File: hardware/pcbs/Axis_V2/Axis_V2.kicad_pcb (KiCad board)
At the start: 2 copper layers, 86.4 x 66 mm, 28 parts, among them J1 SWD, J2 UART, J3 Conn_01x02, J4 Conn_01x02, J5 Conn_01x04, J6 Conn_01x10, J7 Conn_01x08, SW1 RES, U1 Pico, U2 MAX31855EASA, U3 MAX31855EASA, U4 MAX6107, U5 FM24CL16B, U6 ADS1119IPWR, U7 TCA9534

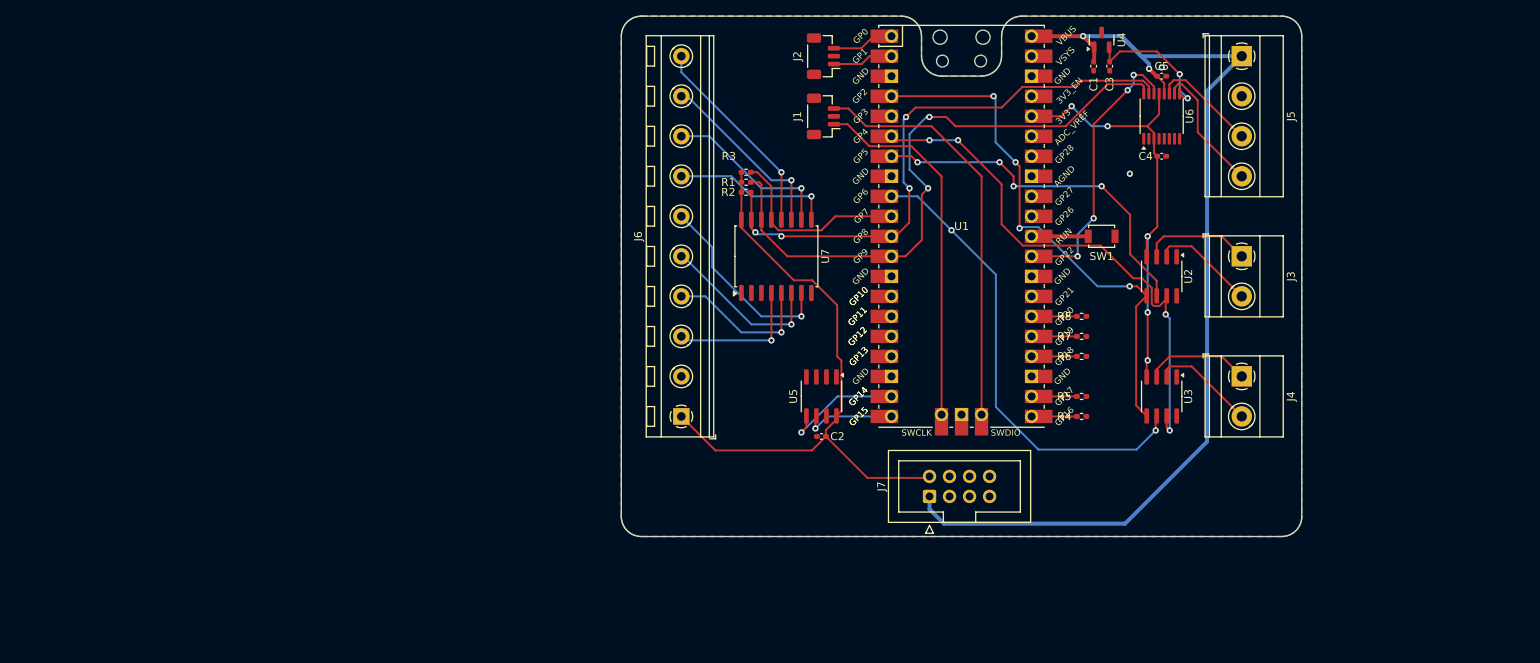
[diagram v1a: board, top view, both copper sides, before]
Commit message: Added a I2C expander for non-essential peripherals, etc.
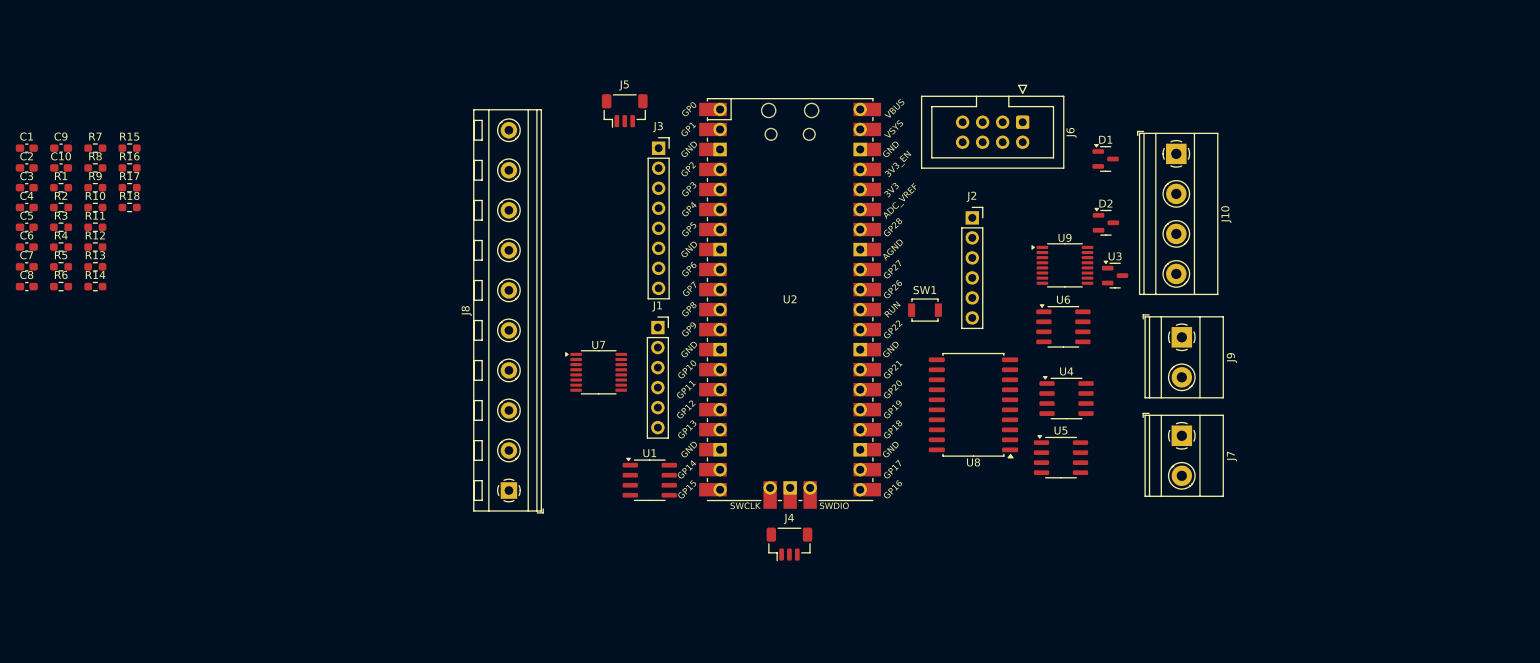
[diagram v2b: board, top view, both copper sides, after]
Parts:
- added C10: 0.1u, Capacitor_SMD:C_0603_1608Metric_Pad1.08x0.95mm_HandSolder, F.Cu at (-13.6, 39.3)
- added C6: 0.1u, Capacitor_SMD:C_0603_1608Metric_Pad1.08x0.95mm_HandSolder, F.Cu at (-18.0, 49.3)
- added C7: 0.1u, Capacitor_SMD:C_0603_1608Metric_Pad1.08x0.95mm_HandSolder, F.Cu at (-18.0, 51.8)
- added C8: 0.1u, Capacitor_SMD:C_0603_1608Metric_Pad1.08x0.95mm_HandSolder, F.Cu at (-18.0, 54.3)
- added C9: 0.1u, Capacitor_SMD:C_0603_1608Metric_Pad1.08x0.95mm_HandSolder, F.Cu at (-13.6, 36.8)
- added D1: 4.7v, Package_TO_SOT_SMD:SOT-23, F.Cu at (118.9, 38.1)
- added D2: 4.7v, Package_TO_SOT_SMD:SOT-23, F.Cu at (119.0, 46.2)
- added J10: Conn_01x04, TerminalBlock_Phoenix:TerminalBlock_Phoenix_MKDS-1,5-4-5.08_1x04_P5.08mm_Horizontal, F.Cu at (127.9, 37.5)
- added J8: Conn_01x10, TerminalBlock_RND:TerminalBlock_RND_205-00240_1x10_P5.08mm_Horizontal, F.Cu at (43.2, 80.2)
- added J9: Conn_01x02, TerminalBlock_Phoenix:TerminalBlock_Phoenix_MKDS-1,5-2-5.08_1x02_P5.08mm_Horizontal, F.Cu at (128.6, 60.8)
- added R10: 1k, Resistor_SMD:R_0603_1608Metric_Pad0.98x0.95mm_HandSolder, F.Cu at (-9.29, 44.3)
- added R11: 1k, Resistor_SMD:R_0603_1608Metric_Pad0.98x0.95mm_HandSolder, F.Cu at (-9.29, 46.8)
- added R12: 1k, Resistor_SMD:R_0603_1608Metric_Pad0.98x0.95mm_HandSolder, F.Cu at (-9.29, 49.3)
- added R13: 1k, Resistor_SMD:R_0603_1608Metric_Pad0.98x0.95mm_HandSolder, F.Cu at (-9.29, 51.8)
- added R14: 1k, Resistor_SMD:R_0603_1608Metric_Pad0.98x0.95mm_HandSolder, F.Cu at (-9.29, 54.3)
- added R15: 1k, Resistor_SMD:R_0603_1608Metric_Pad0.98x0.95mm_HandSolder, F.Cu at (-4.94, 36.8)
- added R16: 1k, Resistor_SMD:R_0603_1608Metric_Pad0.98x0.95mm_HandSolder, F.Cu at (-4.94, 39.3)
- added R17: 1k, Resistor_SMD:R_0603_1608Metric_Pad0.98x0.95mm_HandSolder, F.Cu at (-4.94, 41.8)
- added R18: 1k, Resistor_SMD:R_0603_1608Metric_Pad0.98x0.95mm_HandSolder, F.Cu at (-4.94, 44.3)
- added R9: 1k, Resistor_SMD:R_0603_1608Metric_Pad0.98x0.95mm_HandSolder, F.Cu at (-9.29, 41.8)
- added U8: PCA9544AD, Package_SO:SOIC-20W_7.5x12.8mm_P1.27mm, F.Cu at (102.2, 69.3)
- added U9: ADS1119IPWR, Package_SO:TSSOP-16_4.4x5mm_P0.65mm, F.Cu at (113.8, 51.6)
- C1, C2, C3, C4, C5: footprint Capacitor_SMD:C_0402_1005Metric_Pad0.74x0.62mm_HandSolder -> Capacitor_SMD:C_0603_1608Metric_Pad1.08x0.95mm_HandSolder
- J1: value SWD -> EXT_SPI; footprint Connector_JST:JST_SH_BM03B-SRSS-TB_1x03-1MP_P1.00mm_Vertical -> Connector_PinSocket_2.54mm:PinSocket_1x06_P2.54mm_Vertical
- J2: value UART -> EXT_I2C; footprint Connector_JST:JST_SH_BM03B-SRSS-TB_1x03-1MP_P1.00mm_Vertical -> Connector_PinSocket_2.54mm:PinSocket_1x06_P2.54mm_Vertical
- J3: value Conn_01x02 -> GPIO; footprint TerminalBlock_Phoenix:TerminalBlock_Phoenix_MKDS-1,5-2-5.08_1x02_P5.08mm_Horizontal -> Connector_PinSocket_2.54mm:PinSocket_1x08_P2.54mm_Vertical
- J4: value Conn_01x02 -> SWD; footprint TerminalBlock_Phoenix:TerminalBlock_Phoenix_MKDS-1,5-2-5.08_1x02_P5.08mm_Horizontal -> Connector_JST:JST_SH_BM03B-SRSS-TB_1x03-1MP_P1.00mm_Vertical
- J5: value Conn_01x04 -> UART; footprint TerminalBlock_Phoenix:TerminalBlock_Phoenix_MKDS-1,5-4-5.08_1x04_P5.08mm_Horizontal -> Connector_JST:JST_SH_BM03B-SRSS-TB_1x03-1MP_P1.00mm_Vertical
- J6: value Conn_01x10 -> HV_IDC; footprint TerminalBlock_RND:TerminalBlock_RND_205-00240_1x10_P5.08mm_Horizontal -> Connector_IDC:IDC-Header_2x04_P2.54mm_Vertical
- J7: value Conn_01x08 -> Conn_01x02; footprint Connector_IDC:IDC-Header_2x04_P2.54mm_Vertical -> TerminalBlock_Phoenix:TerminalBlock_Phoenix_MKDS-1,5-2-5.08_1x02_P5.08mm_Horizontal
- R1, R2, R3, R4, R5, R6, R7, R8: footprint Resistor_SMD:R_0402_1005Metric_Pad0.72x0.64mm_HandSolder -> Resistor_SMD:R_0603_1608Metric_Pad0.98x0.95mm_HandSolder
- U1: value Pico -> FM24CL16B; footprint MCU_RaspberryPi_and_Boards:RPi_Pico_SMD_TH -> Package_SO:SOIC-8_3.9x4.9mm_P1.27mm
- U2: value MAX31855EASA -> Pico; footprint Package_SO:SOIC-8_3.9x4.9mm_P1.27mm -> MCU_RaspberryPi_and_Boards:RPi_Pico_SMD_TH
- U3: value MAX31855EASA -> MAX6107; footprint Package_SO:SOIC-8_3.9x4.9mm_P1.27mm -> Package_TO_SOT_SMD:SOT-23
- U4: value MAX6107 -> MAX31855EASA; footprint Package_TO_SOT_SMD:SOT-23 -> Package_SO:SOIC-8_3.9x4.9mm_P1.27mm
- U5: value FM24CL16B -> MAX31855EASA
- U6: value ADS1119IPWR -> DS3231MZ; footprint Package_SO:TSSOP-16_4.4x5mm_P0.65mm -> Package_SO:SOIC-8_3.9x4.9mm_P1.27mm
- U7: footprint Package_SO:SOIC-16W_7.5x10.3mm_P1.27mm -> Package_SO:TSSOP-16_4.4x5mm_P0.65mm
- moved C5 145.3 mm to (-18.0, 46.8)
- moved C4 144.2 mm to (-18.0, 44.3)
- moved C3 138.3 mm to (-18.0, 41.8), turned to 0 degrees
- moved C1 135.8 mm to (-18.0, 36.8), turned to 0 degrees
- moved R4 131.3 mm to (-13.6, 49.3), turned to 0 degrees
- moved R5 130.6 mm to (-13.6, 51.8), turned to 0 degrees
- moved R6 129.8 mm to (-13.6, 54.3), turned to 0 degrees
- moved R7 127.4 mm to (-9.29, 36.8), turned to 0 degrees
- moved R8 126.6 mm to (-9.29, 39.3), turned to 0 degrees
- moved C2 106.5 mm to (-18.0, 39.3), turned to 0 degrees
- moved R3 87.2 mm to (-13.6, 46.8)
- moved R2 87.0 mm to (-13.6, 44.3)
- moved R1 86.9 mm to (-13.6, 41.8)
- moved J5 78.6 mm to (57.9, 32.0), turned to 0 degrees
- moved J3 75.3 mm to (62.2, 36.8), turned to 0 degrees
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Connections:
- net /ADC_3 renamed +BATT
- C1 pad 1: +5V -> +3V3
- C2 pad 1: +3V3 -> +5V
- C5 pad 1: +5V -> +3V3
- J1 pad 1: /SWCLK -> +3V3
- J1 pad 2: GND -> /~{SPI1_CS0}
- J1 pad 3: /SWDIO -> /SPI1_SCK
- J2 pad 1: /UART_RX -> +5V
- J2 pad 2: GND -> +3V3
- J2 pad 3: /UART_TX -> /EXT_SDA
- J3 pad 1: /THCPL1_POS -> +3V3
- J3 pad 2: /THCPL1_NEG -> /GPIO2
- J4 pad 1: /THCPL2_POS -> /SWCLK
- J4 pad 2: /THCPL2_NEG -> GND
- J5 pad 1: +5V -> /UART_RX
- J5 pad 3: /ADC_0 -> /UART_TX
- J6 pad 1: +3V3 -> +5V
- J6 pad 2: GND -> +3V3
- J6 pad 3: /IO_1 -> /EXT_PWR
- J6 pad 4: /IO_2 -> /ZC_SIG
- J6 pad 5: /IO_3 -> /HV_SDA
- J6 pad 6: /IO_4 -> /HV_SCL
- J6 pad 7: /IO_5 -> /~{HV_INT}
- J6 pad 8: /IO_6 -> GND
- J7 pad 1: +5V -> /THCPL2_POS
- J7 pad 2: +3V3 -> /THCPL2_NEG
- R1 pad 2: /I2C0_SCL -> /I2C0_SDA
- R2 pad 2: /I2C0_SDA -> /I2C1_SDA
- R3 pad 2: /~{I2C0_IO_INT} -> /I2C0_SCL
- R4 pad 1: Net-(J7-Pin_3) -> +3V3
- R4 pad 2: /HV_IO1 -> /I2C1_SCL
- R5 pad 1: Net-(J7-Pin_4) -> +3V3
- R5 pad 2: /HV_IO2 -> /~{IO_INT}
- R6 pad 1: Net-(J7-Pin_5) -> +3V3
- R6 pad 2: /HV_IO3 -> /~{MUX_INT}
- R7 pad 1: Net-(J7-Pin_6) -> +3V3
- R7 pad 2: /HV_IO4 -> /HV_SDA
- R8 pad 1: Net-(J7-Pin_7) -> +3V3
- R8 pad 2: /HV_IO5 -> /HV_SCL
- SW1 pad 2: Net-(U1-RUN) -> Net-(U2-RUN)
- U1 pad 1: /UART_TX -> unconnected-(U1-Pad1)
- U1 pad 2: /UART_RX -> unconnected-(U1-Pad2)
- U1 pad 3: GND -> unconnected-(U1-Pad3)
- U1 pad 4: /SPI0_SCK -> GND
- U1 pad 5: unconnected-(U1-GPIO3-Pad5) -> /I2C0_SDA
- U1 pad 6: /SPI0_RX -> /I2C0_SCL
- U1 pad 7: /SPI0_CS0 -> GND
- U1 pad 8: GND -> +3V3
- U2 pad 1: GND -> /UART_TX
- U2 pad 2: /THCPL1_NEG -> /UART_RX
- U2 pad 3: /THCPL1_POS -> GND
- U2 pad 4: +3V3 -> /GPIO2
- U2 pad 5: /SPI0_SCK -> /GPIO3
- U2 pad 6: /SPI0_CS0 -> /GPIO4
- U2 pad 7: /SPI0_RX -> /GPIO5
- U2 pad 8: (no net) -> GND
- U3 pad 1: GND -> +5V
- U3 pad 2: /THCPL2_NEG -> /4.5V_VREF
- U3 pad 3: /THCPL2_POS -> GND
- U4 pad 1: +5V -> GND
- U4 pad 2: /4.5V_VREF -> /THCPL1_NEG
- U4 pad 3: GND -> /THCPL1_POS
- U5 pad 1: unconnected-(U5-Pad1) -> GND
- U5 pad 2: unconnected-(U5-Pad2) -> /THCPL2_NEG
- U5 pad 3: unconnected-(U5-Pad3) -> /THCPL2_POS
- U5 pad 4: GND -> +3V3
- U5 pad 5: /I2C1_SDA -> /SPI0_SCK
- U5 pad 6: /I2C1_SCL -> /~{SPI0_CS1}
- U5 pad 7: GND -> /SPI0_RX
- U5 pad 8: +3V3 -> (no net)
- U6 pad 1: GND -> unconnected-(U6-32KHZ-Pad1)
- U6 pad 2: GND -> +3V3
- U6 pad 3: +3V3 -> /~{TIMER_INT}
- U6 pad 4: GND -> unconnected-(U6-~{RST}-Pad4)
- U6 pad 7: /ADC_2 -> /TIMER_SDA
- U6 pad 8: GND -> /TIMER_SCL
- U7 pad 13: /~{I2C0_IO_INT} -> /~{IO_INT}
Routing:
- net +5V: track 133.8 -> 0.00 mm, vias 2 -> 0
- net +3V3: track 133.8 -> 0.00 mm, vias 5 -> 0
- net /I2C0_SCL: track 78.9 -> 0.00 mm, vias 2 -> 0
- net /I2C0_SDA: track 73.6 -> 0.00 mm, vias 4 -> 0
- net /SPI0_RX: track 68.2 -> 0.00 mm, vias 4 -> 0
- net /SPI0_SCK: track 67.2 -> 0.00 mm, vias 4 -> 0
- net /SPI0_CS1: track 59.6 -> 0.00 mm, vias 2 -> 0
- net /SWDIO: track 52.6 -> 0.00 mm
- net /SWCLK: track 46.6 -> 0.00 mm
- net /SPI0_CS0: track 45.8 -> 0.00 mm, vias 4 -> 0
- net /~{I2C0_ADS_RDY}: track 35.9 -> 0.00 mm, vias 4 -> 0
- net /IO_8: track 26.0 -> 0.00 mm, vias 1 -> 0
- net /IO_4: track 25.0 -> 0.00 mm, vias 1 -> 0
- net /~{I2C0_IO_INT}: track 24.3 -> 0.00 mm
- net /IO_7: track 23.4 -> 0.00 mm, vias 1 -> 0
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- removed copper zone on B.Cu, net GND
- removed copper zone on F.Cu, net GND
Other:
- board outline removed
- board text removed: "GP10"
- board text removed: "GP11"
- board text removed: "GP12"
- board text removed: "GP13"
- board text removed: "GP14"
- board text removed: "GP15"

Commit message: Almost done with v2, getting design review
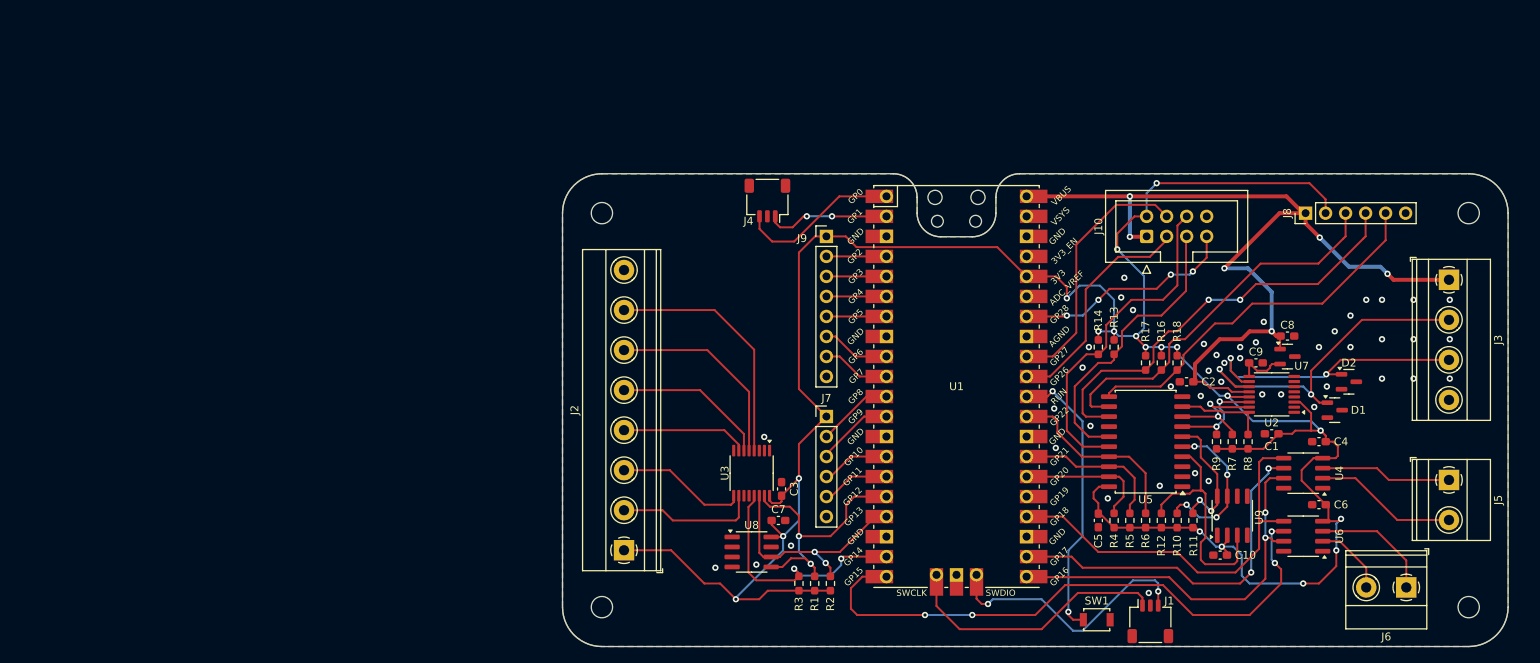
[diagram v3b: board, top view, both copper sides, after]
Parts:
- removed R15: 1k, Resistor_SMD:R_0603_1608Metric_Pad0.98x0.95mm_HandSolder
- added H1: MountingHole, MountingHole:MountingHole_2.7mm_M2.5, F.Cu at (55.0, 45.0)
- added H2: MountingHole, MountingHole:MountingHole_2.7mm_M2.5, F.Cu at (55.0, 95.0)
- added H3: MountingHole, MountingHole:MountingHole_2.7mm_M2.5, F.Cu at (165.0, 45.0)
- added H4: MountingHole, MountingHole:MountingHole_2.7mm_M2.5, F.Cu at (165.0, 95.0)
- J1: renamed from J4; footprint Connector_JST:JST_SH_BM03B-SRSS-TB_1x03-1MP_P1.00mm_Vertical -> Connector_JST:JST_SH_SM03B-SRSS-TB_1x03-1MP_P1.00mm_Horizontal
- J2: renamed from J8; value Conn_01x10 -> GPIO; footprint TerminalBlock_RND:TerminalBlock_RND_205-00240_1x10_P5.08mm_Horizontal -> TerminalBlock_Phoenix:TerminalBlock_Phoenix_MKDS-1,5-8-5.08_1x08_P5.08mm_Horizontal
- J4: renamed from J5; footprint Connector_JST:JST_SH_BM03B-SRSS-TB_1x03-1MP_P1.00mm_Vertical -> Connector_JST:JST_SH_SM03B-SRSS-TB_1x03-1MP_P1.00mm_Horizontal
- J7: renamed from J1; footprint Connector_PinSocket_2.54mm:PinSocket_1x06_P2.54mm_Vertical -> Connector_PinHeader_2.54mm:PinHeader_1x06_P2.54mm_Vertical
- J8: renamed from J2; footprint Connector_PinSocket_2.54mm:PinSocket_1x06_P2.54mm_Vertical -> Connector_PinHeader_2.54mm:PinHeader_1x06_P2.54mm_Vertical
- J9: renamed from J3; footprint Connector_PinSocket_2.54mm:PinSocket_1x08_P2.54mm_Vertical -> Connector_PinHeader_2.54mm:PinHeader_1x08_P2.54mm_Vertical
- moved C6 167.2 mm to (146.0, 82.0), turned to 180 degrees
- moved C4 166.7 mm to (146.0, 74.0), turned to 180 degrees
- moved C1 162.1 mm to (140.0, 73.0), turned to 180 degrees
- moved C8 160.1 mm to (142.0, 60.6)
- moved C10 155.1 mm to (133.5, 88.4), turned to 180 degrees
- moved C9 154.1 mm to (138.0, 64.0)
- moved R8 150.4 mm to (137.0, 74.0), turned to 90 degrees
- moved C2 149.7 mm to (129.2, 66.4), turned to 180 degrees
- moved R7 149.0 mm to (135.0, 74.0), turned to 90 degrees
- moved R9 145.9 mm to (133.0, 74.0), turned to 90 degrees
- moved R11 144.2 mm to (130.0, 84.0), turned to 90 degrees
- moved R10 142.9 mm to (128.0, 84.0), turned to 90 degrees
- moved C5 141.0 mm to (118.0, 84.0), turned to -90 degrees
- moved R6 140.8 mm to (124.0, 84.0), turned to 90 degrees
- moved R5 140.0 mm to (122.0, 84.0), turned to 90 degrees
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- renumbered J6 to J10, J10 to J3, J9 to J5, J7 to J6, R3 to R2, R5 to R3, R2 to R4, R4 to R5, U2 to U1, U9 to U2, U7 to U3, U8 to U5, U5 to U6, U3 to U7, U1 to U8, U6 to U9
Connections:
- net /EXT_PWR renamed /HV_IO1
- C10 pad 1: +5V -> +3V3
- C3 pad 1: /4.5V_VREF -> +3V3
- C8 pad 1: +3V3 -> +5V
- C9 pad 1: +3V3 -> /4.5V_VREF
- J10 pad 7: /~{HV_INT} -> /HV_IO2
- J2 pad 2: /IO_1 -> /IO_6
- J2 pad 3: /IO_2 -> /IO_5
- J2 pad 4: /IO_3 -> /IO_4
- J2 pad 5: /IO_4 -> /IO_3
- J2 pad 6: /IO_5 -> /IO_2
- J2 pad 7: /IO_6 -> /IO_1
- J2 pad 8: /IO_7 -> GND
- J7 pad 2: /~{SPI1_CS0} -> /SPI1_RX
- J7 pad 3: /SPI1_SCK -> /~{SPI1_CS0}
- J7 pad 4: /SPI1_TX -> /SPI1_SCK
- J7 pad 5: /SPI1_RX -> /SPI1_TX
- R10 pad 2: /ADS_SDA -> /TIMER_SDA
- R11 pad 2: /EXT_SDA -> /TIMER_SCL
- R12 pad 2: /TIMER_SDA -> /~{TIMER_INT}
- R13 pad 2: /ADS_SCL -> /HV_SDA
- R14 pad 2: /EXT_SCL -> /HV_SCL
- R16 pad 2: /~{ADS_RDY} -> /EXT_SDA
- R17 pad 2: /~{EXT_INT} -> /EXT_SCL
- R18 pad 2: /~{TIMER_INT} -> /~{EXT_INT}
- R7 pad 2: /HV_SDA -> /ADS_SDA
- R8 pad 2: /HV_SCL -> /ADS_SCL
- R9 pad 2: /~{HV_INT} -> /~{ADS_RDY}
- U1 pad 34: unconnected-(U2-GPIO28_ADC2-Pad34)_1 -> /HV_IO2
- U3 pad 11: /IO_7 -> unconnected-(U3-P6-Pad11)
- U3 pad 12: /IO_8 -> unconnected-(U3-P7-Pad12)
- U5 pad 14: /~{HV_INT} -> unconnected-(U5-~{INT3}-Pad14)
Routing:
- net +3V3: track 0.00 -> 321.9 mm, vias 0 -> 19
- net +5V: track 0.00 -> 115.7 mm, vias 0 -> 6
- net /~{SPI0_CS1}: track 0.00 -> 76.1 mm, vias 0 -> 4
- net /SPI0_SCK: track 0.00 -> 54.7 mm
- net /EXT_SCL: track 0.00 -> 54.6 mm, vias 0 -> 2
- net /SPI0_RX: track 0.00 -> 49.8 mm, vias 0 -> 2
- net /EXT_SDA: track 0.00 -> 48.8 mm
- net /~{EXT_INT}: track 0.00 -> 47.7 mm
- net /~{SPI0_CS0}: track 0.00 -> 46.6 mm, vias 0 -> 2
- net /ADC_0: track 0.00 -> 43.5 mm, vias 0 -> 2
- net /HV_SCL: track 0.00 -> 43.0 mm
- net /HV_SDA: track 0.00 -> 37.3 mm
- net /ADC_1: track 0.00 -> 37.0 mm, vias 0 -> 2
- net Net-(U1-RUN): track 0.00 -> 36.5 mm, vias 0 -> 2
- net /I2C0_SDA: track 0.00 -> 34.5 mm, vias 0 -> 2
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- added copper zone on B.Cu, net GND
- added copper zone on F.Cu, net GND
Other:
- board outline added: 120 x 60 mm

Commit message: Updates
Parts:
- moved J6 11.0 mm to (147.0, 88.1), turned to 0 degrees
- moved D2 7.07 mm to (144.8, 61.4)
- moved C1 7.07 mm to (135.0, 68.0)
- moved C10 7.07 mm to (128.5, 83.4)
- moved C3 7.07 mm to (72.8, 75.0)
- moved C4 7.07 mm to (141.0, 69.0)
- moved C5 7.07 mm to (113.0, 79.0)
- moved C6 7.07 mm to (141.0, 77.0)
- moved C7 7.07 mm to (72.4, 79.0)
- moved C8 7.07 mm to (137.0, 55.6)
- moved C9 7.07 mm to (133.0, 59.0)
- moved D1 7.07 mm to (143.0, 65.0)
- moved H1 7.07 mm to (50.0, 40.0)
- moved H2 7.07 mm to (50.0, 90.0)
- moved H3 7.07 mm to (160.0, 40.0)
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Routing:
- net /THCPL2_NEG: track 9.42 -> 13.3 mm
- net /THCPL2_POS: track 15.6 -> 12.3 mm, vias 0 -> 2
- net +3V3: track 321.9 -> 325.0 mm
- net /THCPL1_POS: track 16.6 -> 19.5 mm, vias 0 -> 2
- net /THCPL1_NEG: track 18.2 -> 16.7 mm
- net /~{SPI0_CS0}: track 46.6 -> 47.9 mm
- net /IO_2: track 25.5 -> 24.2 mm
- net /~{TIMER_INT}: track 30.4 -> 31.6 mm
- net /4.5V_VREF: track 6.53 -> 7.66 mm
- net +5V: track 115.7 -> 114.7 mm
- net /SPI0_SCK: track 54.7 -> 55.5 mm
- net GND: vias 46 -> 48

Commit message: Add "V3"
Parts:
- moved J3 14.4 mm to (165.2, 60.7), turned to 90 degrees
- moved C1 7.62 mm to (142.0, 65.0)
- moved C10 7.62 mm to (135.5, 80.4)
- moved C2 7.62 mm to (133.0, 59.4)
- moved C3 7.62 mm to (79.8, 72.0)
- moved C4 7.62 mm to (148.0, 66.0)
- moved C5 7.62 mm to (120.0, 76.0)
- moved C6 7.62 mm to (148.0, 74.0)
- moved C7 7.62 mm to (79.4, 76.0)
- moved C8 7.62 mm to (144.0, 52.6)
- moved C9 7.62 mm to (140.0, 56.0)
- moved D1 7.62 mm to (150.0, 62.0)
- moved D2 7.62 mm to (151.8, 58.4)
- moved H1 7.62 mm to (57.0, 37.0)
- moved H2 7.62 mm to (57.0, 87.0)
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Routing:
- net /ADC_1: track 37.0 -> 39.8 mm
- net /ADC_0: track 43.5 -> 46.3 mm, vias 2 -> 4
- net GND: vias 48 -> 52
